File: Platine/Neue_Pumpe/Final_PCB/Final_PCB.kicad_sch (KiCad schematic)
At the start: 5 parts, among them J1 Conn_01x12, J2 Conn_01x01

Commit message: a lot of advance in final PCB
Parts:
- added J3, J5: Conn_01x10, FLE-105-01-G-DV-K-TR:FLE-105-01-X-DV-Y-TR, symbol Connector_Generic:Conn_01x10
- added J4: Conn_01x10, Samtec-FTSH-105-01-L-DV-K:FTSH-105-01-L-DV-K, symbol Connector_Generic:Conn_01x10
- added J6, J7: Conn_01x06, Connector_PinHeader_1.27mm:PinHeader_2x03_P1.27mm_Vertical_SMD, symbol Connector_Generic:Conn_01x06
- added R55, R56, R57, R58, R59, R60, R61, R62, R63: 12.5, Resistor_SMD:R_0603_1608Metric_Pad0.98x0.95mm_HandSolder, symbol Device:R
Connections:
- net GNDA: now also R55.1, R56.1, R57.1, R58.1, R59.1, R60.1, R61.1, R62.1, R63.1
- new net analog_inp_1: J3.1 (Pin_1), J4.1 (Pin_1), J5.1 (Pin_1), R55.2
- new net analog_inp_2: J3.2 (Pin_2), J4.2 (Pin_2), J5.2 (Pin_2), R56.2
- new net analog_inp_3: J3.3 (Pin_3), J4.3 (Pin_3), J5.3 (Pin_3), R57.2
- new net analog_inp_4: J3.4 (Pin_4), J4.4 (Pin_4), J5.4 (Pin_4), R58.2
- new net analog_inp_5: J3.5 (Pin_5), J4.5 (Pin_5), J5.5 (Pin_5), R59.2
- new net analog_inp_6: J3.6 (Pin_6), J4.6 (Pin_6), J5.6 (Pin_6), R60.2
- new net analog_inp_7: J3.7 (Pin_7), J4.7 (Pin_7), J5.7 (Pin_7), R61.2
- new net analog_inp_8: J3.8 (Pin_8), J4.8 (Pin_8), J5.8 (Pin_8), R62.2
- new net analog_inp_9: J3.9 (Pin_9), J4.9 (Pin_9), J5.9 (Pin_9), R63.2
- no-connect marks 4 -> 7
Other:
- note added: "Anode connectors"
- note added: "Resistors"
- note added: "To-anode connector"
- moved on the sheet: J1, J2

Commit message: still need to finish routing
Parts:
- removed J2: Conn_01x01, symbol Connector_Generic:Conn_01x01
- removed J6: Conn_01x06, Connector_PinHeader_1.27mm:PinHeader_2x03_P1.27mm_Vertical_SMD, symbol Connector_Generic:Conn_01x06
- added J6: Conn_01x08, Connector_PinHeader_1.27mm_modified:PinHeader_2x04_P1.27mm_Vertical_SMD, symbol Connector_Generic:Conn_01x08
- added J8: Conn_01x08, Connector_PinHeader_1.27mm:PinHeader_2x04_P1.27mm_Horizontal, symbol Connector_Generic:Conn_01x08
- added J9: Conn_01x06, Connector_PinHeader_1.27mm:PinHeader_2x03_P1.27mm_Horizontal, symbol Connector_Generic:Conn_01x06
- J1: footprint (none) -> SHF-106-01-L-D-SM:SHF-106-01-L-D-SM
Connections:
- net +3.3VA: now also J6.6 (Pin_6), J8.6 (Pin_6)
- net +3.3VD: now also J1.7 (Pin_7), J7.2 (Pin_2), J9.2 (Pin_2)
- net GNDA: now also J6.8 (Pin_8), J8.8 (Pin_8)
- net GNDD: now also J1.5 (Pin_5), J7.1 (Pin_1), J9.1 (Pin_1)
- net Out1: now also J1.2 (Pin_2)
- net Out2: now also J1.6 (Pin_6)
- net Out3: now also J1.8 (Pin_8)
- net Out4: now also J1.9 (Pin_9)
- net Out5: now also J1.12 (Pin_12)
- net Out6: now also J1.10 (Pin_10)
- net Out7: now also J1.4 (Pin_4)
- net Out8: now also J1.1 (Pin_1)
- net Out9: now also J1.3 (Pin_3)
- net VPlatte(GNDA): now also J1.11 (Pin_11)
- net analog_inp_4: now also J6.4 (Pin_4), J8.4 (Pin_4)
- net analog_inp_8: now also J6.2 (Pin_2), J8.2 (Pin_2)
- net fil_da2: now reaches J7.3 (Pin_3)
- net fil_da2: now also J9.3 (Pin_3)
- net fil_da7: now reaches J7.4 (Pin_4)
- net fil_da7: now also J9.4 (Pin_4)
- net fil_da6: now reaches J7.6 (Pin_6)
- net fil_da6: now also J9.6 (Pin_6)
- new net fil_da1: J6.5 (Pin_5), J8.5 (Pin_5)
- new net fil_da3: J6.3 (Pin_3), J8.3 (Pin_3)
- new net fil_da5: J6.1 (Pin_1), J8.1 (Pin_1)
- new net fil_da9: J6.7 (Pin_7), J8.7 (Pin_7)
- no-connect marks 7 -> 9
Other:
- added sheet Pre-Filter (pre_filter.kicad_sch)
- note added: "Connector from outside"
- note added: "LP+SC PCB to Sensor PCB connectors"
- note added: "Sensor PCB to LP+SC PCB connectors"
- note added: "Shunt resistors"
- note removed: "Resistors"
- note removed: "Stecker (von draußen)"
- moved on the sheet: J1

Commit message: Almost done with routing
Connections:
- net VPlatte(GNDA) is gone; now on net GNDA: J1.11 (Pin_11)
- net +3.3VA: now also J8.4 (Pin_4); no longer J8.6 (Pin_6)
- net GNDA: now also J8.2 (Pin_2); no longer J8.8 (Pin_8)
- net analog_inp_4: now also J8.6 (Pin_6); no longer J8.4 (Pin_4)
- net analog_inp_8: now also J8.8 (Pin_8); no longer J8.2 (Pin_2)
- net fil_da1: now also J7.5 (Pin_5), J9.5 (Pin_5); no longer J8.5 (Pin_5)
- net fil_da3: now also J8.5 (Pin_5); no longer J8.3 (Pin_3)
- net fil_da5: now also J8.7 (Pin_7); no longer J8.1 (Pin_1)
- net fil_da9: now also J8.1 (Pin_1); no longer J8.7 (Pin_7)
- no-connect marks 9 -> 8
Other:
- note added: "GNDA -> VPlatte"

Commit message: final PCB finished
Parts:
- added J2: Conn_01x10, FLE-105-01-G-DV-K-TR:FLE-105-01-X-DV-Y-TR, symbol Connector_Generic:Conn_01x10
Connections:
- net GNDD: now also J7.5 (Pin_5), J9.5 (Pin_5); no longer J7.1 (Pin_1), J9.1 (Pin_1)
- net analog_inp_1: now also J2.1 (Pin_1)
- net analog_inp_2: now also J2.2 (Pin_2)
- net analog_inp_3: now also J2.3 (Pin_3)
- net analog_inp_4: now also J2.4 (Pin_4)
- net analog_inp_5: now also J2.5 (Pin_5)
- net analog_inp_6: now also J2.6 (Pin_6)
- net analog_inp_7: now also J2.7 (Pin_7)
- net analog_inp_8: now also J2.8 (Pin_8)
- net analog_inp_9: now also J2.9 (Pin_9)
- net fil_da1: now also J7.1 (Pin_1), J9.1 (Pin_1); no longer J7.5 (Pin_5), J9.5 (Pin_5)
- no-connect marks 8 -> 9
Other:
- moved on the sheet: J1, J4, J6, J7, J8, J9

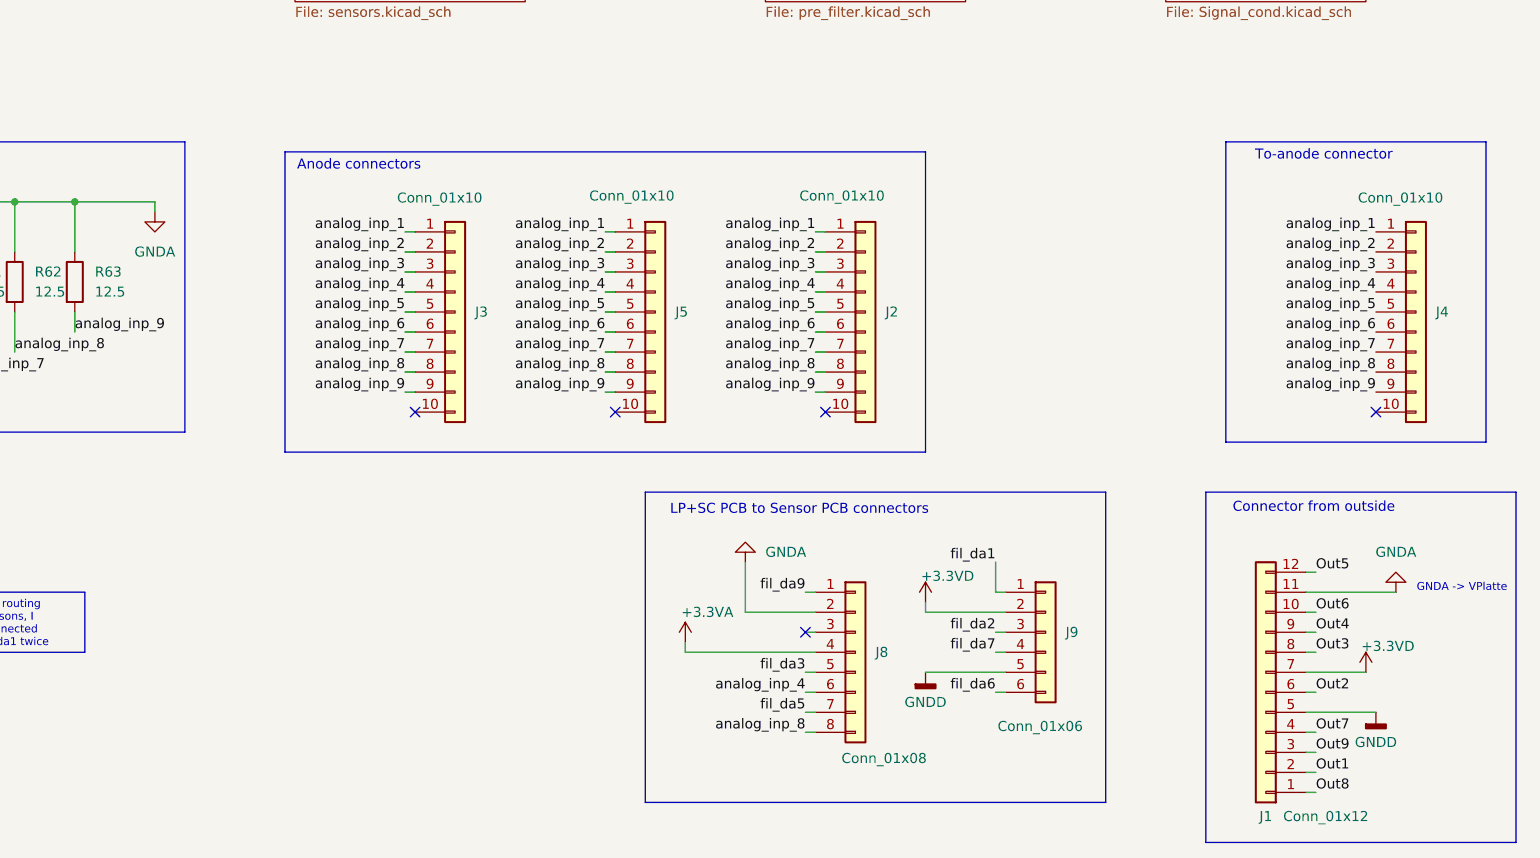
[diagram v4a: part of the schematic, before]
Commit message: Added grid voltage connector
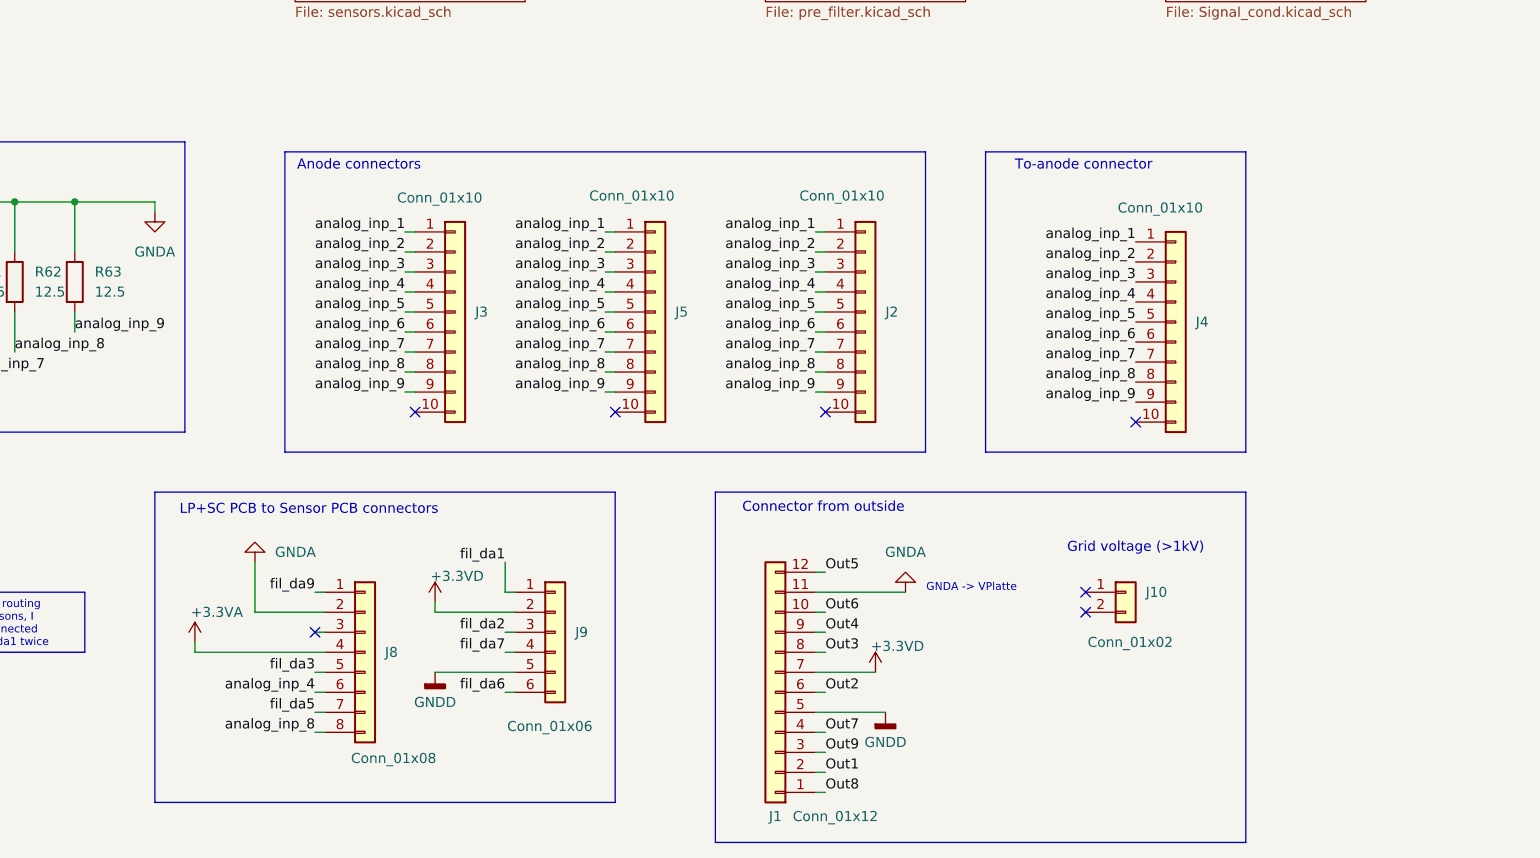
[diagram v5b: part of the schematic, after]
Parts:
- added J10: Conn_01x02, OSTTE020104:OST_OSTTE020104, symbol Connector_Generic:Conn_01x02
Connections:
- no-connect marks 9 -> 11
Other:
- note added: "Grid voltage (>1kV)"
- moved on the sheet: J1, J4, J8, J9

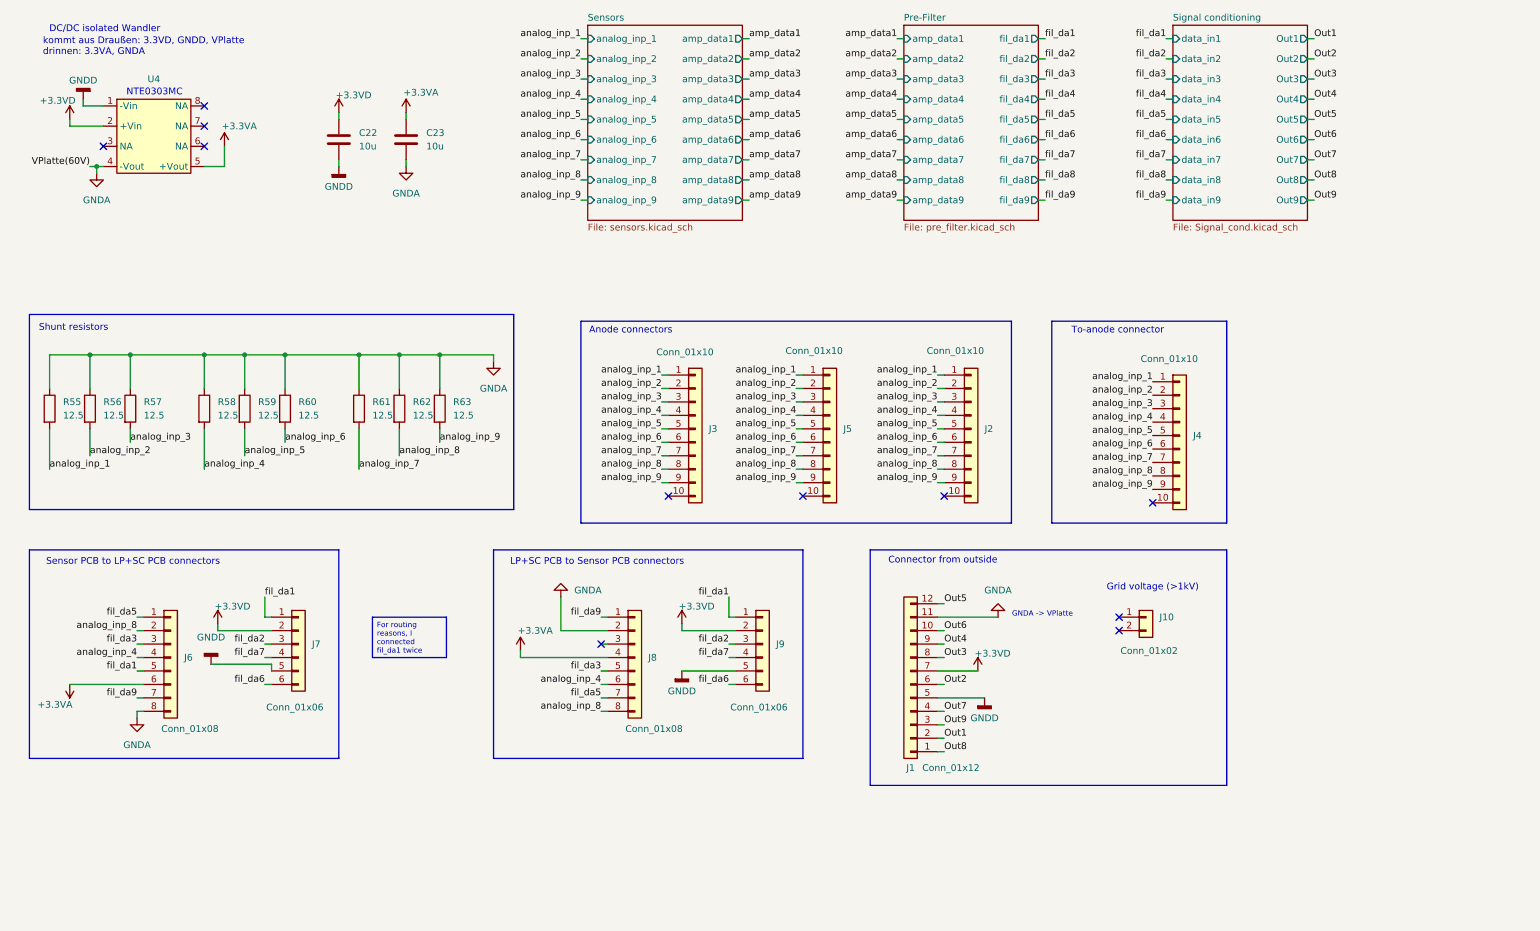
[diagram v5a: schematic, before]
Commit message: Commit before changing PCB connectors, just in case
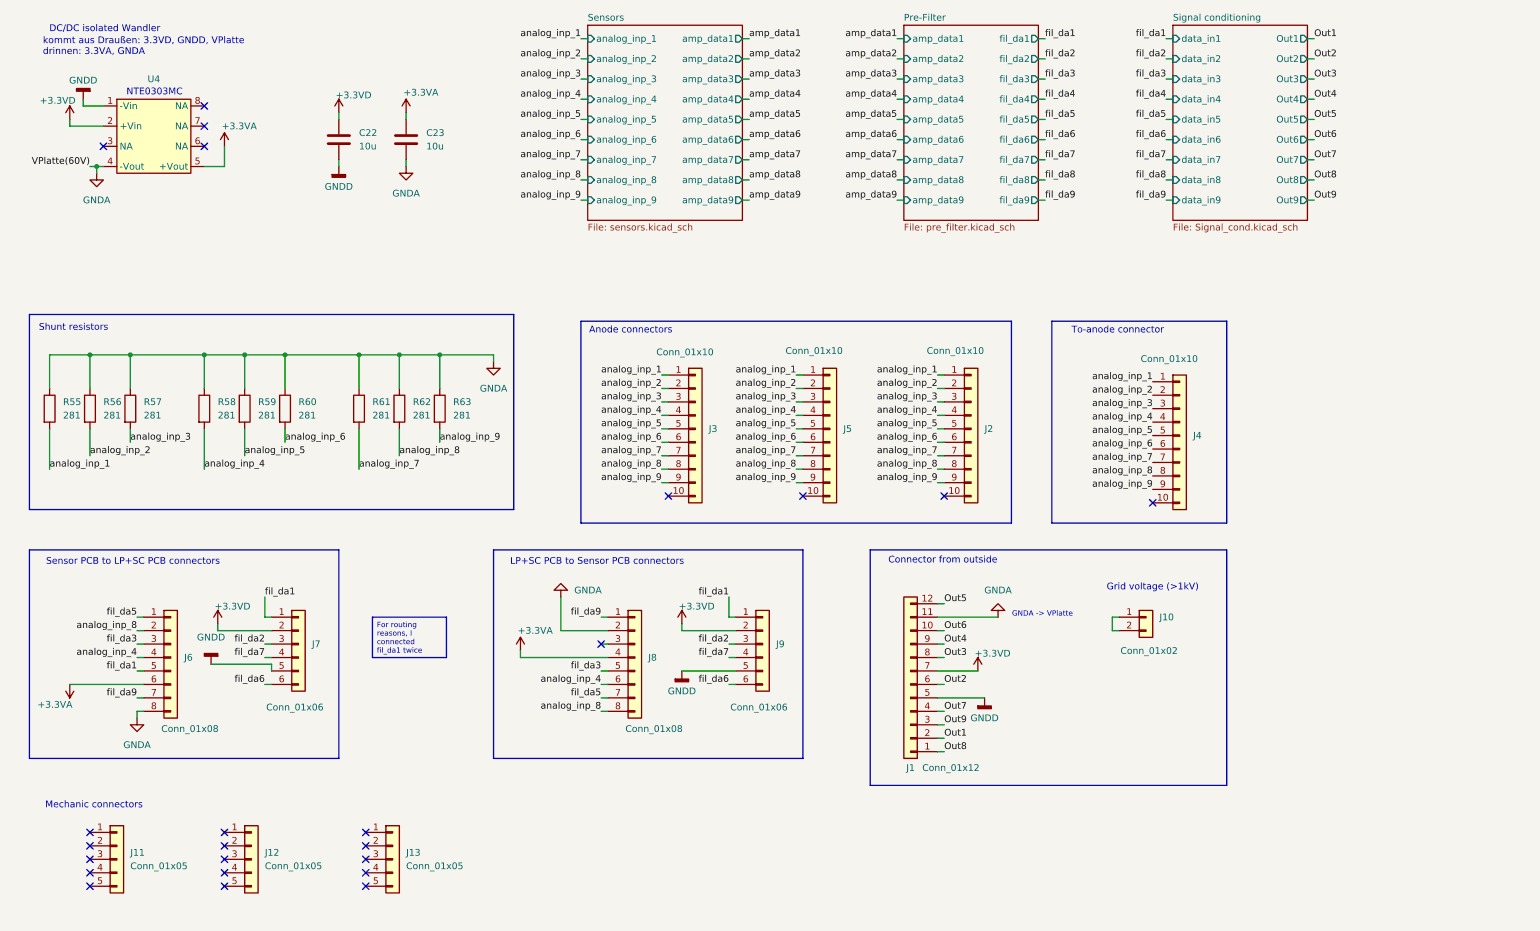
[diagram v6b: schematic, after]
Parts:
- added J11, J12, J13: Conn_01x05, Connector_PinHeader_1.27mm:PinHeader_1x05_P1.27mm_Vertical, symbol Connector_Generic:Conn_01x05
- R55, R56, R57, R58, R59, R60, R61, R62, R63: value 12.5 -> 281
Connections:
- net at J10.1 (Pin_1): now also J10.2 (Pin_2)
- no-connect marks 11 -> 24
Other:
- note added: "Mechanic connectors"
